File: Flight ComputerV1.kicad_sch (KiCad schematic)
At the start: 26 parts, among them J101 ICSP, J102 Screw_Terminal_01x02, J103 Conn_01x08, J104 Conn_01x07, J105 Micro_SD_Card, J106 Conn_02x10_Top_Bottom, SW101 1-1825910-8, U101 ATmega328PB-A, U102 LMT84DCK

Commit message: Testing
Added Title label in schematic
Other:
- title: (none) -> Flight Recorder Mk1
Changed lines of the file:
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@@
 (kicad_sch (version 20211123) (generator eeschema)
   (paper "USLetter")
+  (title_block
+    (title "Flight Recorder Mk1")
+    (rev "2")
+  )
   (junction (at 136.525 154.305) (diameter 0) (color 0 0 0 0)
   )
@@
       (reference "#PWR0121") (unit 1) (value "GNDPWR") (footprint "")
     )
-    (path "/05ad3611-bc85-4d66-85e8-c067f8cfca78/50ab12ea-f9dd-4fb6-bfa6-9de4f2f08388"
-      (reference "#PWR0122") (unit 1) (value "GND") (footprint "")
-    )
     (path "/05ad3611-bc85-4d66-85e8-c067f8cfca78/b83d40be-f6a9-41a0-b4b1-8341ddbca8b8"

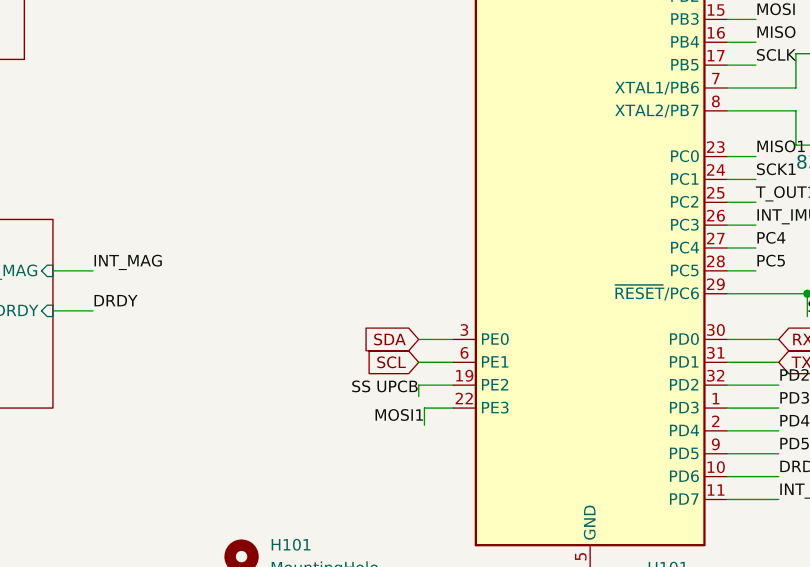
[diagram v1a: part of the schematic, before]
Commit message: added pullup resistors
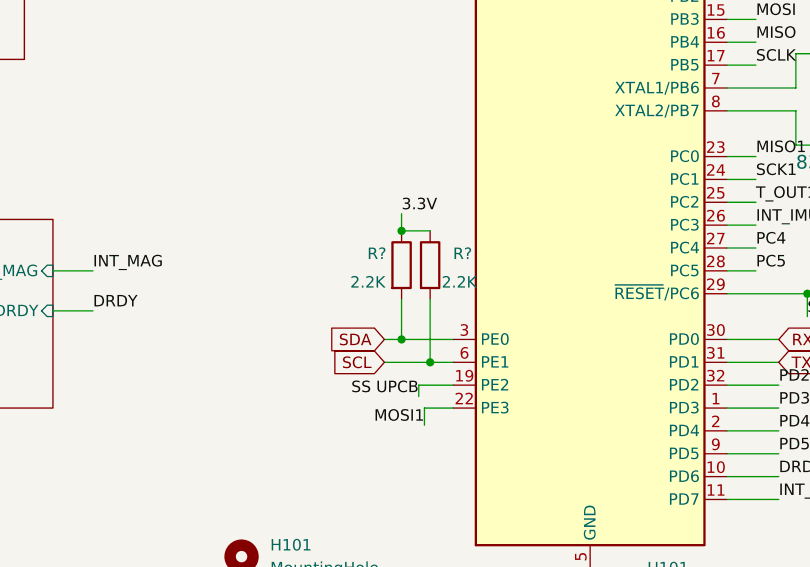
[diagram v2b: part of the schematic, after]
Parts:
- added R? (x2): 2.2K, Resistor_SMD:R_0603_1608Metric_Pad0.98x0.95mm_HandSolder, symbol Device:R
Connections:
- net 3.3V: now also R?.1, R?.1
- net SCL: now also R?.2
- net SDA: now also R?.2
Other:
- title: Flight Recorder Mk1 -> (none)
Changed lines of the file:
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@@
 (kicad_sch (version 20211123) (generator eeschema)
   (paper "USLetter")
-  (title_block
-    (title "Flight Recorder Mk1")
-    (rev "2")
-  )
   (junction (at 136.525 154.305) (diameter 0) (color 0 0 0 0)
   )
+  (junction (at 114.935 95.25) (diameter 0) (color 0 0 0 0)
+  )
+  (junction (at 114.935 83.185) (diameter 0) (color 0 0 0 0)
+  )
   (junction (at 117.475 40.64) (diameter 0) (color 0 0 0 0)
   )
@@
   (junction (at 135.89 40.64) (diameter 0) (color 0 0 0 0)
   )
+  (junction (at 118.11 97.79) (diameter 0) (color 0 0 0 0)
+  )
   (junction (at 219.71 54.61) (diameter 0) (color 0 0 0 0)
   )
@@
     (stroke (width 0) (type default) (color 0 0 0 0))
   )
+  (wire (pts (xy 114.935 83.185) (xy 118.11 83.185))
+    (stroke (width 0) (type default) (color 0 0 0 0))
+  )
   (wire (pts (xy 160.02 90.17) (xy 160.02 92.71))
     (stroke (width 0) (type default) (color 0 0 0 0))
@@
     (stroke (width 0) (type default) (color 0 0 0 0))
   )
+  (wire (pts (xy 114.935 90.805) (xy 114.935 95.25))
+    (stroke (width 0) (type default) (color 0 0 0 0))
+  )
   (wire (pts (xy 151.13 113.03) (xy 156.845 113.03))
     (stroke (width 0) (type default) (color 0 0 0 0))
@@
     (stroke (width 0) (type default) (color 0 0 0 0))
   )
+  (wire (pts (xy 118.11 97.79) (xy 120.65 97.79))
+    (stroke (width 0) (type default) (color 0 0 0 0))
+  )
   (wire (pts (xy 117.475 38.1) (xy 117.475 40.64))
     (stroke (width 0) (type default) (color 0 0 0 0))
@@
     (stroke (width 0) (type default) (color 0 0 0 0))
   )
+  (wire (pts (xy 118.11 90.805) (xy 118.11 97.79))
+    (stroke (width 0) (type default) (color 0 0 0 0))
+  )
   (wire (pts (xy 219.71 38.1) (xy 223.52 38.1))
     (stroke (width 0) (type default) (color 0 0 0 0))
@@
     (stroke (width 0) (type default) (color 0 0 0 0))
   )
+  (wire (pts (xy 114.935 95.25) (xy 120.65 95.25))
+    (stroke (width 0) (type default) (color 0 0 0 0))
+  )
   (wire (pts (xy 135.89 38.735) (xy 135.89 40.64))
     (stroke (width 0) (type default) (color 0 0 0 0))
@@
     (stroke (width 0) (type default) (color 0 0 0 0))
   )
-  (wire (pts (xy 116.84 95.25) (xy 120.65 95.25))
+  (wire (pts (xy 113.03 95.25) (xy 114.935 95.25))
     (stroke (width 0) (type default) (color 0 0 0 0))
   )
@@
     (stroke (width 0) (type default) (color 0 0 0 0))
   )
+  (wire (pts (xy 114.935 81.28) (xy 114.935 83.185))
+    (stroke (width 0) (type default) (color 0 0 0 0))
+  )
   (wire (pts (xy 69.85 176.53) (xy 76.835 176.53))
     (stroke (width 0) (type default) (color 0 0 0 0))
@@
     (stroke (width 0) (type default) (color 0 0 0 0))
   )
-  (wire (pts (xy 116.84 97.79) (xy 120.65 97.79))
+  (wire (pts (xy 113.03 97.79) (xy 118.11 97.79))
     (stroke (width 0) (type default) (color 0 0 0 0))
   )
@@
   (label "SCLK" (at 188.595 128.905 180)
     (effects (font (size 1.27 1.27)) (justify right bottom))
+  )
+  (label "3.3V" (at 114.935 81.28 0)
+    (effects (font (size 1.27 1.27)) (justify left bottom))
   )
   (label "INT_MAG" (at 156.845 113.03 0)
@@
     )
   )
-  (global_label "SCL" (shape input) (at 116.84 97.79 180) (fields_autoplaced)
+  (global_label "SCL" (shape input) (at 113.03 97.79 180) (fields_autoplaced)
     (effects (font (size 1.27 1.27)) (justify right))
-    (property "Intersheet References" "${INTERSHEET_REFS}" (id 0) (at 110.9193 97.7106 0)
+    (property "Intersheet References" "${INTERSHEET_REFS}" (id 0) (at 107.1093 97.7106 0)
       (effects (font (size 1.27 1.27)) (justify right) hide)
     )
@@
     )
   )
-  (global_label "SDA" (shape input) (at 116.84 95.25 180) (fields_autoplaced)
+  (global_label "SDA" (shape input) (at 113.03 95.25 180) (fields_autoplaced)
     (effects (font (size 1.27 1.27)) (justify right))
-    (property "Intersheet References" "${INTERSHEET_REFS}" (id 0) (at 110.8588 95.1706 0)
+    (property "Intersheet References" "${INTERSHEET_REFS}" (id 0) (at 107.0488 95.1706 0)
       (effects (font (size 1.27 1.27)) (justify right) hide)
     )
@@
     )
     (property "Datasheet" "https://www.digikey.com/en/products/detail/sunled/XZVG55W-1/4745973" (id 3) (at 126.365 28.575 0)
+      (effects (font (size 1.27 1.27)) hide)
+    )
+    (pin "1")
+    (pin "2")
+  )
+  (symbol (lib_id "Device:R") (at 118.11 86.995 0) (unit 1)
+    (in_bom yes) (on_board yes)
+    (property "Reference" "R?" (id 0) (at 120.65 85.7249 0)
+      (effects (font (size 1.27 1.27)) (justify left))
+    )
+    (property "Value" "2.2K" (id 1) (at 119.38 88.9 0)
+      (effects (font (size 1.27 1.27)) (justify left))
+    )
+    (property "Footprint" "Resistor_SMD:R_0603_1608Metric_Pad0.98x0.95mm_HandSolder" (id 2) (at 116.332 86.995 90)
+      (effects (font (size 1.27 1.27)) hide)
+    )
+    (property "Datasheet" "~" (id 3) (at 118.11 86.995 0)
       (effects (font (size 1.27 1.27)) hide)
     )
@@
     (pin "9")
   )
+  (symbol (lib_id "Device:R") (at 114.935 86.995 0) (unit 1)
+    (in_bom yes) (on_board yes)
+    (property "Reference" "R?" (id 0) (at 111.125 85.725 0)
+      (effects (font (size 1.27 1.27)) (justify left))
+    )
+    (property "Value" "2.2K" (id 1) (at 109.22 88.9 0)
+      (effects (font (size 1.27 1.27)) (justify left))
+    )
+    (property "Footprint" "Resistor_SMD:R_0603_1608Metric_Pad0.98x0.95mm_HandSolder" (id 2) (at 113.157 86.995 90)
+      (effects (font (size 1.27 1.27)) hide)
+    )
+    (property "Datasheet" "~" (id 3) (at 114.935 86.995 0)
+      (effects (font (size 1.27 1.27)) hide)
+    )
+    (pin "1")
+    (pin "2")
+  )
   (symbol (lib_id "power:GND") (at 50.165 171.45 270) (unit 1)
     (in_bom yes) (on_board yes)
@@
       (reference "#PWR0121") (unit 1) (value "GNDPWR") (footprint "")
     )
+    (path "/05ad3611-bc85-4d66-85e8-c067f8cfca78/50ab12ea-f9dd-4fb6-bfa6-9de4f2f08388"
+      (reference "#PWR0122") (unit 1) (value "GND") (footprint "")
+    )
     (path "/05ad3611-bc85-4d66-85e8-c067f8cfca78/b83d40be-f6a9-41a0-b4b1-8341ddbca8b8"
       (reference "#PWR0123") (unit 1) (value "GND") (footprint "")
@@
       (reference "R104") (unit 1) (value "10k") (footprint "Resistor_SMD:R_0603_1608Metric_Pad0.98x0.95mm_HandSolder")
     )
+    (path "/6d16946f-e7e3-4057-a77a-a59e185720b7"
+      (reference "R?") (unit 1) (value "2.2K") (footprint "Resistor_SMD:R_0603_1608Metric_Pad0.98x0.95mm_HandSolder")
+    )
+    (path "/e5b78b0a-74e7-4c16-9c80-d38293fc0eb8"
+      (reference "R?") (unit 1) (value "2.2K") (footprint "Resistor_SMD:R_0603_1608Metric_Pad0.98x0.95mm_HandSolder")
+    )
     (path "/adfa3d90-c58c-4aef-bda7-bc6239b73083"

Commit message: updates to schematics
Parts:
- C104: value 0.1uF -> 100nF
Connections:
- net T_OUT1: no longer C105.1, U102.3 (OUT)
- new net: C105.1, U102.3 (OUT)
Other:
- moved on the sheet: C104, C105, H101, H102, H103, H104, J101, J102, J103, J104, J105, J106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
